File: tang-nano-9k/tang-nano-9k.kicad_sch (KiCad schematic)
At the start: 3 parts

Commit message: Updated schematic
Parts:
- removed U?: W5500_Breakout, symbol fpca:W5500_Breakout
- added C1, C2, C3, C4: 100n, symbol Device:C_Small
- added C5: 10u, symbol Device:C_Polarized_Small
- added C6: 22u, symbol Device:C_Polarized_Small
- added J1: UART_header, symbol fpca:UART_header
- added J2: Mini-DIN-6, symbol Connector:Mini-DIN-6
- added J3: Trackball_breakout, symbol fpca:Trackball_breakout
- added J4: BBQ10KBD_PMOD, symbol fpca:BBQ10KBD_PMOD
- added R1, R2, R3, R4, R5, R6, R7: 1k, symbol Device:R
- added R10, R11, R13, R8: 200k, symbol Device:R
- added R12, R14, R15, R16, R17, R18, R9: 2k2, symbol Device:R
- added U10: AZ117, symbol fpca:AZ117
- added U2: W5500_Breakout, symbol fpca:W5500_Breakout
- added U4, U7, U8, U9: GTL2002, symbol fpca:GTL2002
- added U5: I2C_OLED, symbol fpca:I2C_OLED
- added U6: TCA9538, symbol fpca:TCA9538
- gave numbers to parts that had none: 2
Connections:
- net ETH_RST: now reaches U1.10 (30/IOB13B)
- net ETH_RST: now also U2.8 (RST)
- net +3V3: now reaches U1.25 (3V3)
- net +3V3: now also U3.7 (Rout), C5.1, J3.11 (VCC), J4.6 (3V3), R11.1, R13.1, R14.1, R15.1, R17.1, R18.1, R8.1, R9.1, U10.3 (INPUT), U2.10 (3V3), U2.11 (3V3), U5.2 (VCC), U6.16 (VCC), U6.3 (RESETn)
- net GND: now reaches U1.26 (GND)
- net GND: now also U3.1 (SCLK), U3.14 (3V0), U3.2 (SF1), U3.4 (SF0), U3.6 (DEEM), U3.9 (Lout), C1.2, C2.2, C3.2, C4.2, C5.2, C6.2, J1.3 (GND), J2.3, J3.10 (GND), J4.5 (GND), U10.1 (ADJ/GND), U2.1 (GND), U2.12 (GND), U2.2 (GND), U4.1 (GND), U5.1 (GND), U6.1 (A0), U6.2 (A1), U6.8 (GND), U7.1 (GND), U8.1 (GND), U9.1 (GND)
- net UART_TX: now reaches U1.27 (32/IOB15B/RGB_TOUCH_XR)
- net UART_TX: now also J1.1 (TX)
- net UART_RX: now reaches U1.28 (31/IOB15A/RGB_TOUCH_YD)
- net UART_RX: now also J1.2 (RX)
- net SDA: now reaches U1.29 (49/IOR24A/SPILCD_RS)
- net SDA: now also J4.4 (SDA), U5.4 (SDA), U6.15 (SDA)
- net SCL: now reaches U1.30 (48/IOR24B/SPILCD_CS)
- net SCL: now also J4.3 (SCL), U5.3 (SCL), U6.14 (SCL)
- net +5V: now reaches U1.31 (5V)
- net +5V: now also J2.4, R10.1, R12.1, R16.1
- net I2S_WSEL: now reaches U1.38 (76/IOT37B/SPILCD_CK)
- net I2S_WSEL: now also U3.10 (BCLK)
- net I2S_DATA: now reaches U1.39 (77/IOT37A/SPILCD_MO)
- net I2S_DATA: now also U3.11 (DIN)
- net PS2_CLK_1V8: now reaches U1.40 (79/IOT12B)
- net PS2_CLK_1V8: now also R2.1, U7.3 (S1)
- net PS2_DATA_1V8: now reaches U1.41 (80/IOT12A)
- net PS2_DATA_1V8: now also R4.2, U7.4 (S2)
- net TRACKBALL_LFT_1V8: now reaches U1.42 (81/IOT11B)
- net TRACKBALL_LFT_1V8: now also R3.1, U8.3 (S1)
- net TRACKBALL_RHT_1V8: now reaches U1.43 (82/IOT11A)
- net TRACKBALL_RHT_1V8: now also R6.2, U8.4 (S2)
- net TRACKBALL_UP_1V8: now reaches U1.44 (83/IOT10B)
- net TRACKBALL_UP_1V8: now also R5.1, U9.3 (S1)
- net TRACKBALL_DWN_1V8: now reaches U1.45 (84/IOT10A)
- net TRACKBALL_DWN_1V8: now also R7.2, U9.4 (S2)
- net GPIO_INTn_1V8: now reaches U1.46 (85/IOT8B)
- net GPIO_INTn_1V8: now also R1.1, U4.3 (S1)
- net I2S_BCLK: now reaches U1.48 (63/IOR5A/RGB_TOUCH_XL)
- net I2S_BCLK: now also U3.12 (WSEL)
- net ETH_INT: now reaches U1.5 (25/IOB8A)
- net ETH_INT: now also U2.6 (INT)
- net ETH_MISO: now reaches U1.6 (26/IOB8B)
- net ETH_MISO: now also U2.7 (MISO)
- net ETH_MOSI: now reaches U1.7 (27/IOB11A)
- net ETH_MOSI: now also U2.3 (MOSI)
- net ETH_SCK: now reaches U1.8 (28/IOB11B)
- net ETH_SCK: now also U2.4 (SCK)
- net ETH_CS: now reaches U1.9 (29/IOB13A)
- net ETH_CS: now also U2.5 (CS)
- net AUDIO_SF0: now reaches U3.3 (MUTE)
- net AUDIO_SF0: now also U6.9 (P4)
- net AUDIO_SF1: now reaches U3.5 (PLL)
- net AUDIO_SF1: now also U6.10 (P5)
- new net: C3.1, R11.2, U8.7 (DREF), U8.8 (GREF)
- new net: C1.1, R8.2, U4.7 (DREF), U4.8 (GREF)
- new net: C4.1, R13.2, U9.7 (DREF), U9.8 (GREF)
- new net: C2.1, R10.2, U7.7 (DREF), U7.8 (GREF)
- new net +1V8: C6.1, R1.2, R2.2, R3.2, R4.1, R5.2, R6.1, R7.1, U10.2 (OUTPUT), U4.2 (SREF), U7.2 (SREF), U8.2 (SREF), U9.2 (SREF)
- new net BBQ10KBD_INT: J4.1 (INT), U6.11 (P6)
- new net BLU: J3.1 (BLU), U6.6 (P2)
- new net GPIO_INTn_3V3: R9.2, U4.6 (D1), U6.13 (INTn)
- new net GRN: J3.3 (GRN), U6.5 (P1)
- new net PS2_CLK: J2.5, R12.2, U7.6 (D1)
- new net PS2_DATA: J2.1, R16.2, U7.5 (D2)
- new net RED: J3.2 (RED), U6.4 (P0)
- new net TRACKBALL_BTN: J3.9 (BTN), U6.12 (P7)
- new net TRACKBALL_DWN_3V3: J3.6 (DWN), R18.2, U9.5 (D2)
- new net TRACKBALL_LFT_3V3: J3.7 (LFT), R14.2, U8.6 (D1)
- new net TRACKBALL_RHT_3V3: J3.8 (RHT), R17.2, U8.5 (D2)
- new net TRACKBALL_UP_3V3: J3.5 (UP), R15.2, U9.6 (D1)
- new net WHT: J3.4 (WHT), U6.7 (P3)
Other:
- note added: "3V3->1V8 Level Conversion"
- note added: "Additional desirable interfaces - PS/2 Keyboard/Mouse - Trackball - Audio - Ethernet - small I2C OLED display - additional UART"
- note added: "Audio DAC"
- note added: "Blackberry Keyboard"
- note added: "Ethernet"
- note added: "GPIO Expander"
- note added: "I2C Network"
- note added: "IO Available (when using RGB screen) 3.3V 6 IO +3 for RGB_TOUCH, +4 for the SPI_LCD 13 3.3V IO total usable 7 1.8V IO total usable"
- note added: "OLED Display"
- note added: "PS/2 Keyboard"
- note added: "Tang Nano 9K"
- note added: "These PS/2 pullups may be optional if the keyboard has internal pullups"
- note added: "Trackball"
- note added: "UART"
- note added: "We shouldn't need these 2K2/1K pullups, but the footprints will make useful test points"
- note added: "We will need these 1K pullups"
- note removed: "Additional desirable interfaces - PS/2 Keyboard/Mouse - Trackball - Audio - Ethernet - small I2C OLED display"
- note removed: "IO Available (when not using HDMI) 3.3V 6 IO +3 for RGB_TOUCH, +4 for the SPI_LCD 13 3.3V IO total usable 7 1.8V IO total usable"
- note removed: "Pins Required: 3 Inputs (Optional configuration pins could also be connected)"
- note removed: "Pins Required: 4 Inputs 2 Outputs 6 IO Total"
- company: (none) -> Joseph Hindmarsh
- title: (none) -> Tang Nano 9K Carrier Board
- moved on the sheet: U1, U3

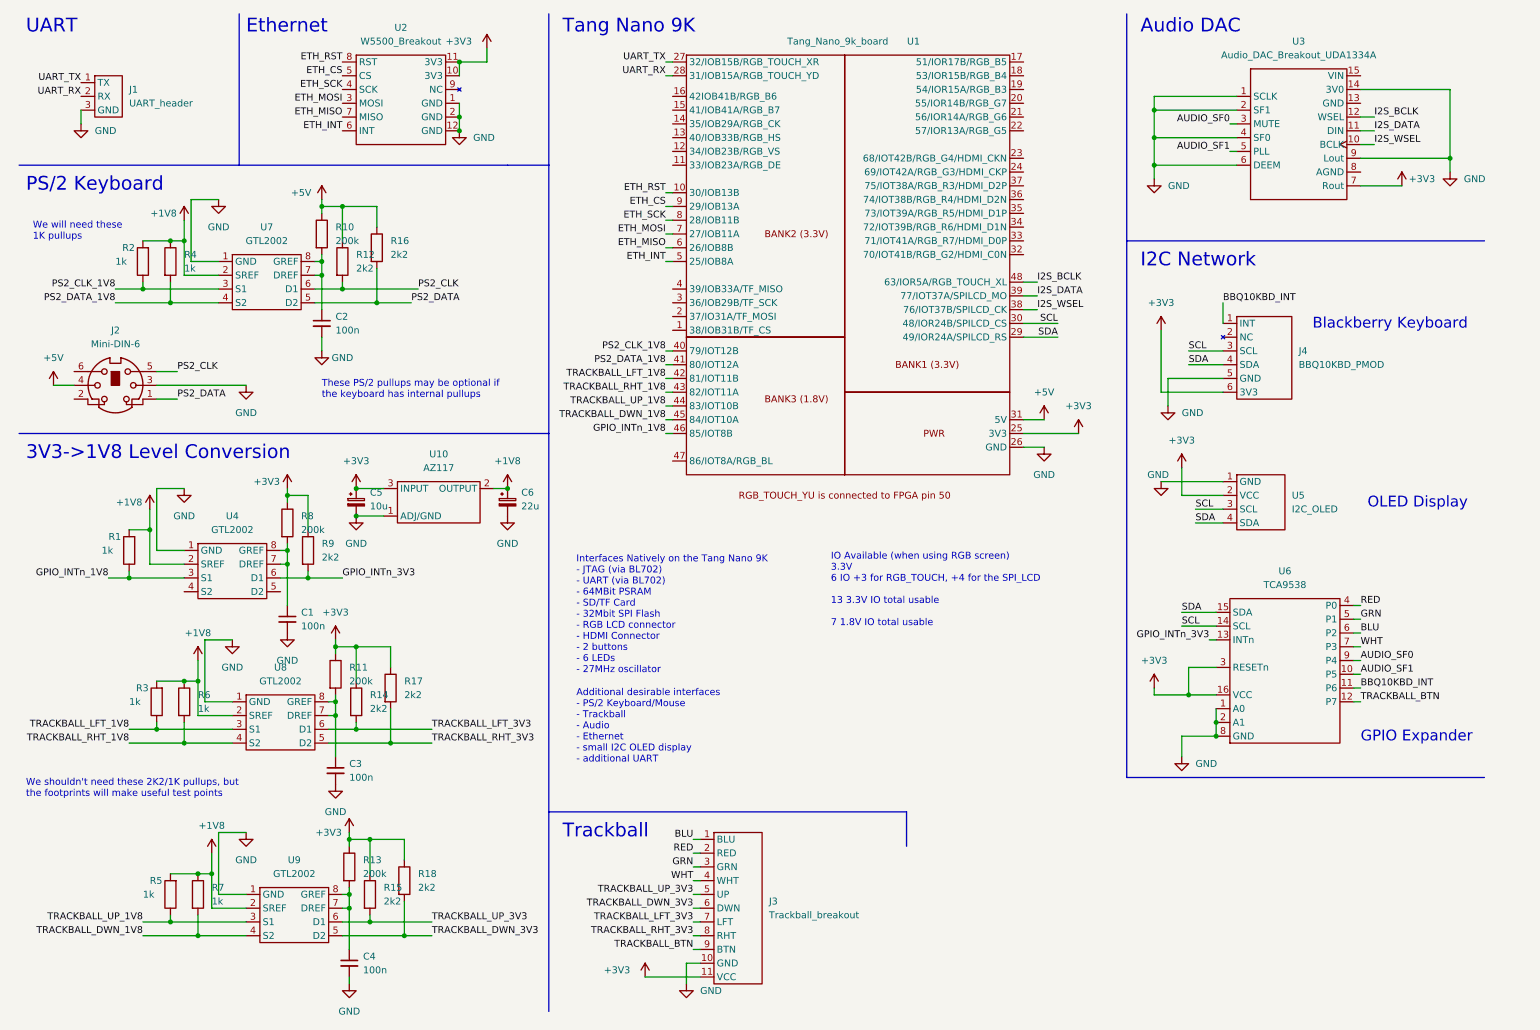
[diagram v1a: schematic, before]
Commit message: fixed UDA1334 connections and added NC to unused pins across the schematic
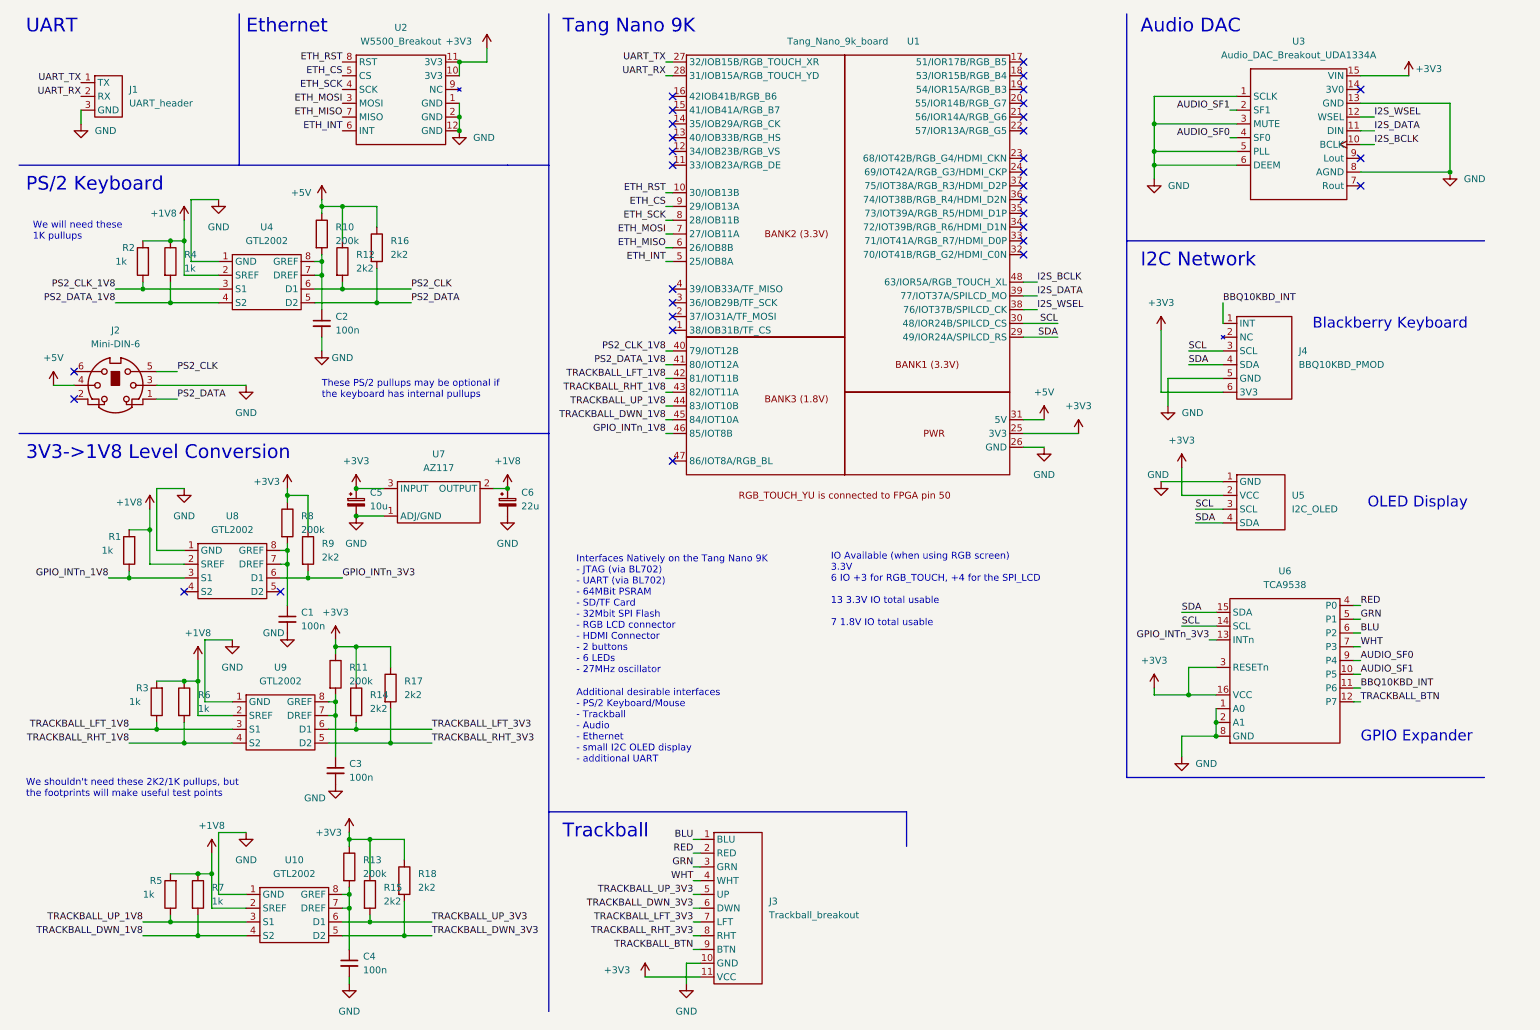
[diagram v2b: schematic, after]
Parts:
- renumbered U9 to U10, U7 to U4, U10 to U7, U4 to U8, U8 to U9
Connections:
- net +3V3: now also U3.15 (VIN); no longer U3.7 (Rout)
- net AUDIO_SF0: now also U3.4 (SF0); no longer U3.3 (MUTE)
- net AUDIO_SF1: now also U3.2 (SF1); no longer U3.5 (PLL)
- net GND: now also U3.13 (GND), U3.3 (MUTE), U3.5 (PLL), U3.8 (AGND); no longer U3.14 (3V0), U3.2 (SF1), U3.4 (SF0), U3.9 (Lout)
- net I2S_BCLK: now also U3.10 (BCLK); no longer U3.12 (WSEL)
- net I2S_WSEL: now also U3.12 (WSEL); no longer U3.10 (BCLK)
- no-connect marks 0 -> 32

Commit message: updated schematic with footprints
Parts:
- removed U7: AZ117, symbol fpca:AZ117
- added R19: 0, Resistor_THT:R_Axial_DIN0204_L3.6mm_D1.6mm_P5.08mm_Horizontal, symbol Device:R
- added U7: AZ1117H-1.8TRE1, Package_TO_SOT_SMD:SOT-223-3_TabPin2, symbol fpca:AZ1117H-1.8TRE1
- C1, C2, C3, C4: footprint (none) -> Capacitor_THT:C_Disc_D3.8mm_W2.6mm_P2.50mm
- C5, C6: footprint (none) -> Capacitor_THT:CP_Radial_D5.0mm_P2.00mm
- J1: footprint (none) -> Connector_PinHeader_2.54mm:PinHeader_1x03_P2.54mm_Vertical
- J2: footprint (none) -> 4x1md_Library:Connector_Mini-DIN_Female_6Pin_2rows
- J3: footprint (none) -> Connector_PinSocket_2.54mm:PinSocket_1x11_P2.54mm_Vertical
- J4: footprint (none) -> Connector_PinHeader_2.54mm:PinHeader_1x06_P2.54mm_Horizontal
- R1, R10, R11, R12, R13, R14, R15, R16, R17, R18, R2, R3, R4, R5, R6, R7, R8, R9: footprint (none) -> Resistor_THT:R_Axial_DIN0207_L6.3mm_D2.5mm_P10.16mm_Horizontal
- U10, U4, U8, U9: footprint (none) -> Package_SO:TSSOP-8_3x3mm_P0.65mm
- U2: footprint (none) -> Custom Library:W5500_Breakout
- U3: footprint (none) -> Custom Library:UDA1334_Breakout
- U5: footprint (none) -> Connector_PinHeader_2.54mm:PinHeader_1x04_P2.54mm_Vertical
- U6: footprint (none) -> Package_SO:SSOP-16_5.3x6.2mm_P0.65mm
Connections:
- net +1V8: now also U7.2 (OUTPUT)
- net +3V3: now also U7.3 (INPUT)
- net GND: now also R19.2, U7.1 (ADJ/GND); no longer U3.8 (AGND)
- new net: R19.1, U3.8 (AGND)
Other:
- note added: "Can optionally tie AGND to GND here"

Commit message: Added pullups to GPIO expander INTn pin Initial placement and partial routing
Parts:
- added R20, R21, R22: 4k7, Resistor_THT:R_Axial_DIN0207_L6.3mm_D2.5mm_P10.16mm_Horizontal, symbol Device:R
- J3: footprint Connector_PinSocket_2.54mm:PinSocket_1x11_P2.54mm_Vertical -> Custom Library:Trackball_breakout
- U5: footprint Connector_PinHeader_2.54mm:PinHeader_1x04_P2.54mm_Vertical -> Custom Library:i2c_oled_128x64
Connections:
- net +3V3: now also R20.1, R21.1, R22.2; no longer U6.3 (RESETn)
- net ETH_INT: now also U1.10 (30/IOB13B); no longer U1.5 (25/IOB8A)
- net ETH_MISO: now also U1.8 (28/IOB11B); no longer U1.6 (26/IOB8B)
- net ETH_MOSI: now also U1.5 (25/IOB8A); no longer U1.7 (27/IOB11A)
- net ETH_RST: now also U1.7 (27/IOB11A); no longer U1.10 (30/IOB13B)
- net ETH_SCK: now also U1.6 (26/IOB8B); no longer U1.8 (28/IOB11B)
- net SCL: now also R21.2
- net SDA: now also R20.2
- new net: R22.1, U6.3 (RESETn)
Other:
- note added: "There are 4k7 pullups on the SDA/SCL lines on the BBQ10KBD PMOD. If we aren't using this, populate the pullups here"
- moved on the sheet: J4
